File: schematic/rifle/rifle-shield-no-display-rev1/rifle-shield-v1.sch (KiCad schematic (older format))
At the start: 39 parts, among them K1 CONN_3, P1 Power, P10 MCU2, P11 RFID-RC522-MODULE, P12 NRF24L01, P13 IR_LED, P15 Vibro&flash, P2 MCU1, P3 Mag&fireMode, P4 VCC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

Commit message: Values of PAM8403 resistors added
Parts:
- C3: value C -> 0.015uF
- R1, R3: value R -> 10k
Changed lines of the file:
@@
 Sheet 1 1
 Title ""
-Date "4 jun 2015"
+Date "11 oct 2015"
 Rev ""
 Comp ""
@@
 P 1950 4750
 F 0 "R3" V 2030 4750 40  0000 C CNN
-F 1 "R" V 1957 4751 40  0000 C CNN
+F 1 "10k" V 1957 4751 40  0000 C CNN
 F 2 "~" V 1880 4750 30  0000 C CNN
 F 3 "~" H 1950 4750 30  0000 C CNN
@@
 P 1450 3000
 F 0 "R1" V 1530 3000 40  0000 C CNN
-F 1 "R" V 1457 3001 40  0000 C CNN
+F 1 "10k" V 1457 3001 40  0000 C CNN
 F 2 "~" V 1380 3000 30  0000 C CNN
 F 3 "~" H 1450 3000 30  0000 C CNN
@@
 P 1450 3500
 F 0 "C3" H 1450 3600 40  0000 L CNN
-F 1 "C" H 1456 3415 40  0000 L CNN
+F 1 "0.015uF" H 1456 3415 40  0000 L CNN
 F 2 "~" H 1488 3350 30  0000 C CNN
 F 3 "~" H 1450 3500 60  0000 C CNN

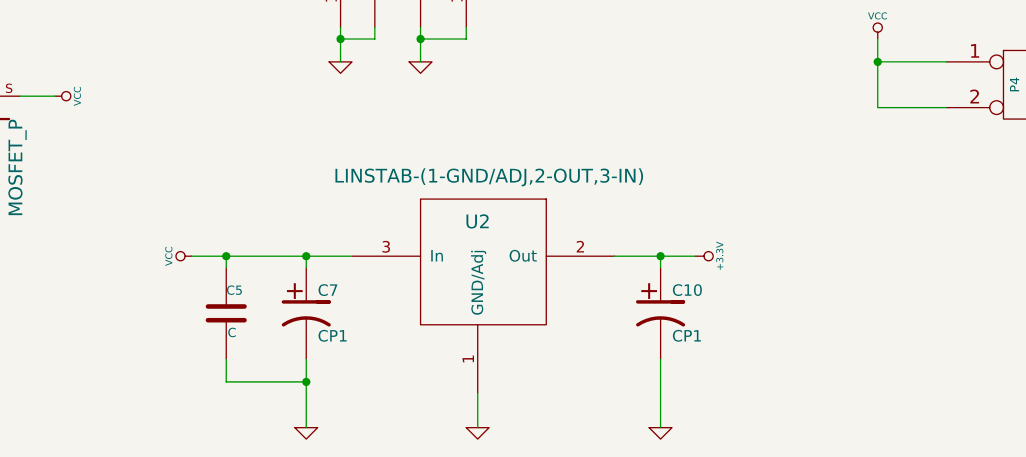
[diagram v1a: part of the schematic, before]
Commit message: Fix for heartbeat; IDC sensor; rifle shield in process
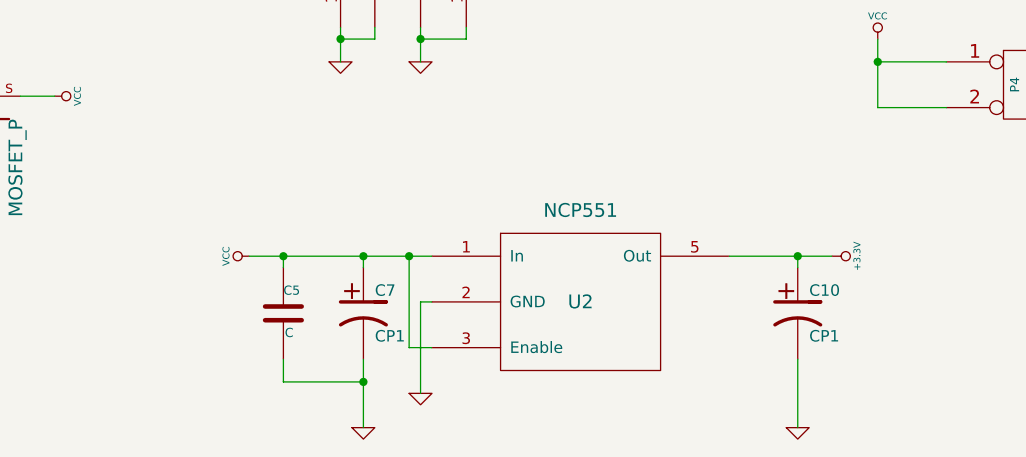
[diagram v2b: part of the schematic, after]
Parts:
- removed U2: LINSTAB-(1-GND/ADJ,2-OUT,3-IN), ~, symbol LINSTAB-(1-GND/ADJ,2-OUT,3-IN)
- added U2: NCP551, ~, symbol NCP551
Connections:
- net +3.3V: now also U2.5 (Out)
- net GND: now also U2.2 (GND)
- net VCC: now also U2.1 (In), U2.3 (Enable)
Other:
- moved on the sheet: C10, C5, C7
